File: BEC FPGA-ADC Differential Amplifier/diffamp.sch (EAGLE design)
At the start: 23 parts, among them U1 ADA4807-2ARMZRM_8-M, X1 22-23-2031, X3 22-23-2021, X4 22-23-2021

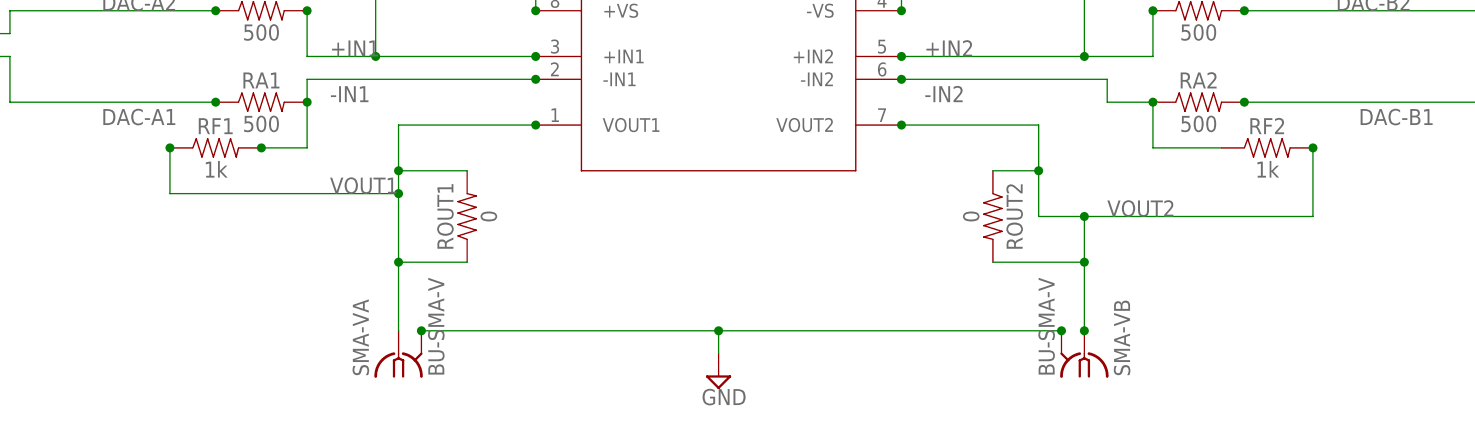
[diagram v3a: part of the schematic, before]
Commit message: Added ground plane and zero ohm resistors. Board Layout modified.
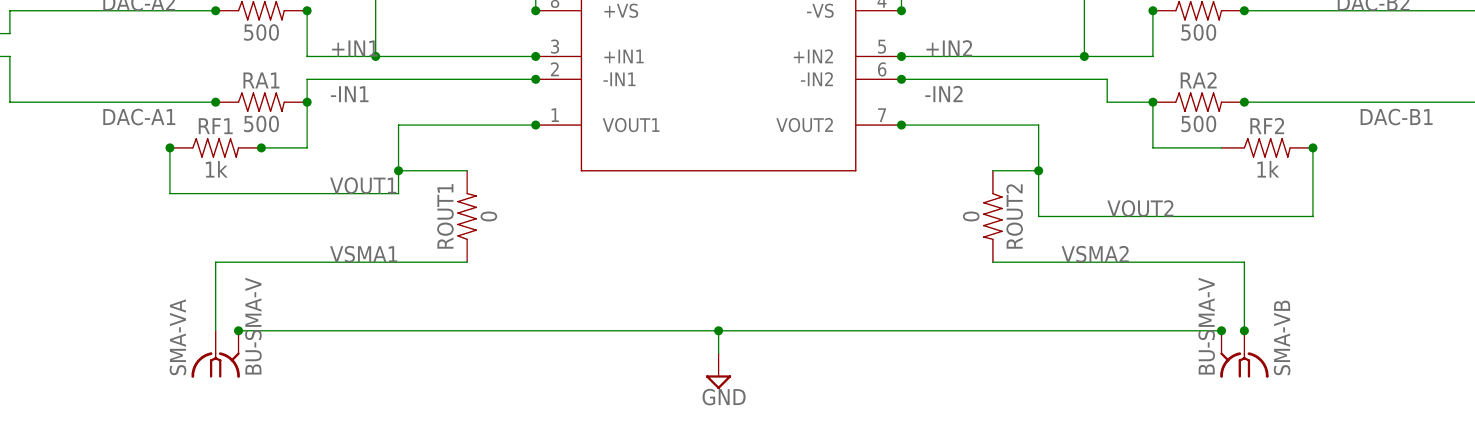
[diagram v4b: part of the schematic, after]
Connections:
- new net VSMA1: ROUT1.1, SMA-VA.1
- new net VSMA2: ROUT2.2, SMA-VB.1
- net VOUT1: no longer ROUT1.1, SMA-VA.1
- net VOUT2: no longer ROUT2.2, SMA-VB.1
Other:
- moved on the sheet: SMA-VA, SMA-VB
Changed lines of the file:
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@@
 <instance part="SUPPLY4" gate="GND" x="53.34" y="73.66" rot="R180"/>
 <instance part="SUPPLY5" gate="GND" x="132.08" y="76.2" rot="R180"/>
-<instance part="SMA-VB" gate="G$1" x="132.08" y="12.7" rot="MR90"/>
-<instance part="SMA-VA" gate="G$1" x="55.88" y="12.7" rot="R90"/>
+<instance part="SMA-VB" gate="G$1" x="149.86" y="12.7" rot="MR90"/>
+<instance part="SMA-VA" gate="G$1" x="35.56" y="12.7" rot="R90"/>
 <instance part="RDC1(DNI)" gate="G$1" x="58.42" y="60.96"/>
 <instance part="RDC2(DNI)" gate="G$1" x="124.46" y="60.96" rot="R180"/>
@@
 <wire x1="55.88" y1="33.02" x2="55.88" y2="38.1" width="0.1524" layer="91"/>
 <wire x1="55.88" y1="38.1" x2="71.12" y2="38.1" width="0.1524" layer="91"/>
-<pinref part="SMA-VA" gate="G$1" pin="1"/>
 <wire x1="30.48" y1="30.48" x2="55.88" y2="30.48" width="0.1524" layer="91"/>
-<wire x1="55.88" y1="15.24" x2="55.88" y2="22.86" width="0.1524" layer="91"/>
-<wire x1="55.88" y1="22.86" x2="55.88" y2="30.48" width="0.1524" layer="91"/>
 <wire x1="30.48" y1="35.56" x2="30.48" y2="30.48" width="0.1524" layer="91"/>
-<junction x="55.88" y="30.48"/>
 <label x="48.26" y="30.48" size="1.778" layer="95"/>
 <junction x="30.48" y="35.56"/>
 <junction x="71.12" y="38.1"/>
-<pinref part="ROUT1" gate="G$1" pin="1"/>
-<wire x1="55.88" y1="22.86" x2="63.5" y2="22.86" width="0.1524" layer="91"/>
-<junction x="55.88" y="22.86"/>
 <pinref part="ROUT1" gate="G$1" pin="2"/>
 <wire x1="63.5" y1="33.02" x2="55.88" y2="33.02" width="0.1524" layer="91"/>
@@
 <segment>
 <pinref part="SMA-VA" gate="G$1" pin="2"/>
-<wire x1="58.42" y1="15.24" x2="91.44" y2="15.24" width="0.1524" layer="91"/>
+<wire x1="38.1" y1="15.24" x2="91.44" y2="15.24" width="0.1524" layer="91"/>
 <wire x1="91.44" y1="15.24" x2="91.44" y2="12.7" width="0.1524" layer="91"/>
 <pinref part="SUPPLY1" gate="GND" pin="GND"/>
 <pinref part="SMA-VB" gate="G$1" pin="2"/>
-<wire x1="91.44" y1="15.24" x2="129.54" y2="15.24" width="0.1524" layer="91"/>
+<wire x1="91.44" y1="15.24" x2="147.32" y2="15.24" width="0.1524" layer="91"/>
 <junction x="91.44" y="15.24"/>
-<junction x="58.42" y="15.24"/>
-<junction x="129.54" y="15.24"/>
+<junction x="38.1" y="15.24"/>
+<junction x="147.32" y="15.24"/>
 </segment>
 <segment>
@@
 <wire x1="127" y1="38.1" x2="127" y2="33.02" width="0.1524" layer="91"/>
 <wire x1="127" y1="33.02" x2="127" y2="27.94" width="0.1524" layer="91"/>
-<wire x1="127" y1="27.94" x2="132.08" y2="27.94" width="0.1524" layer="91"/>
-<wire x1="132.08" y1="27.94" x2="157.48" y2="27.94" width="0.1524" layer="91"/>
+<wire x1="127" y1="27.94" x2="157.48" y2="27.94" width="0.1524" layer="91"/>
 <wire x1="157.48" y1="27.94" x2="157.48" y2="35.56" width="0.1524" layer="91"/>
 <pinref part="RF2" gate="G$1" pin="2"/>
-<pinref part="SMA-VB" gate="G$1" pin="1"/>
-<wire x1="132.08" y1="15.24" x2="132.08" y2="22.86" width="0.1524" layer="91"/>
-<junction x="132.08" y="27.94"/>
 <label x="134.62" y="27.94" size="1.778" layer="95"/>
 <junction x="111.76" y="38.1"/>
 <junction x="157.48" y="35.56"/>
-<junction x="132.08" y="15.24"/>
 <pinref part="ROUT2" gate="G$1" pin="1"/>
-<wire x1="132.08" y1="22.86" x2="132.08" y2="27.94" width="0.1524" layer="91"/>
 <wire x1="121.92" y1="33.02" x2="127" y2="33.02" width="0.1524" layer="91"/>
 <junction x="127" y="33.02"/>
-<pinref part="ROUT2" gate="G$1" pin="2"/>
-<wire x1="121.92" y1="22.86" x2="132.08" y2="22.86" width="0.1524" layer="91"/>
-<junction x="132.08" y="22.86"/>
 </segment>
 </net>
@@
 </segment>
 </net>
+<net name="VSMA1" class="0">
+<segment>
+<pinref part="ROUT1" gate="G$1" pin="1"/>
+<wire x1="35.56" y1="22.86" x2="63.5" y2="22.86" width="0.1524" layer="91"/>
+<pinref part="SMA-VA" gate="G$1" pin="1"/>
+<wire x1="35.56" y1="15.24" x2="35.56" y2="22.86" width="0.1524" layer="91"/>
+<label x="48.26" y="22.86" size="1.778" layer="95"/>
+</segment>
+</net>
+<net name="VSMA2" class="0">
+<segment>
+<pinref part="SMA-VB" gate="G$1" pin="1"/>
+<junction x="149.86" y="15.24"/>
+<wire x1="149.86" y1="15.24" x2="149.86" y2="22.86" width="0.1524" layer="91"/>
+<pinref part="ROUT2" gate="G$1" pin="2"/>
+<wire x1="121.92" y1="22.86" x2="149.86" y2="22.86" width="0.1524" layer="91"/>
+<label x="129.54" y="22.86" size="1.778" layer="95"/>
+</segment>
+</net>

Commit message: Re-routed wires to leave more spacing on PCB.
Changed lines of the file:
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@@
 <net name="-5V" class="0">
 <segment>
-<pinref part="U1" gate="A" pin="-VS"/>
 <pinref part="SUPPLY3" gate="-5V" pin="-5V"/>
-<wire x1="111.76" y1="50.8" x2="111.76" y2="63.5" width="0.1524" layer="91"/>
-<junction x="111.76" y="50.8"/>
 <pinref part="C2" gate="G$1" pin="-"/>
 <wire x1="111.76" y1="63.5" x2="114.3" y2="63.5" width="0.1524" layer="91"/>
@@
 <wire x1="114.3" y1="78.74" x2="114.3" y2="68.58" width="0.1524" layer="91"/>
 <junction x="114.3" y="68.58"/>
+<pinref part="U1" gate="A" pin="-VS"/>
+<wire x1="111.76" y1="63.5" x2="111.76" y2="50.8" width="0.1524" layer="91"/>
 </segment>
 </net>
